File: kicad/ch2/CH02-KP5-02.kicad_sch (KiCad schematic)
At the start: 5 parts

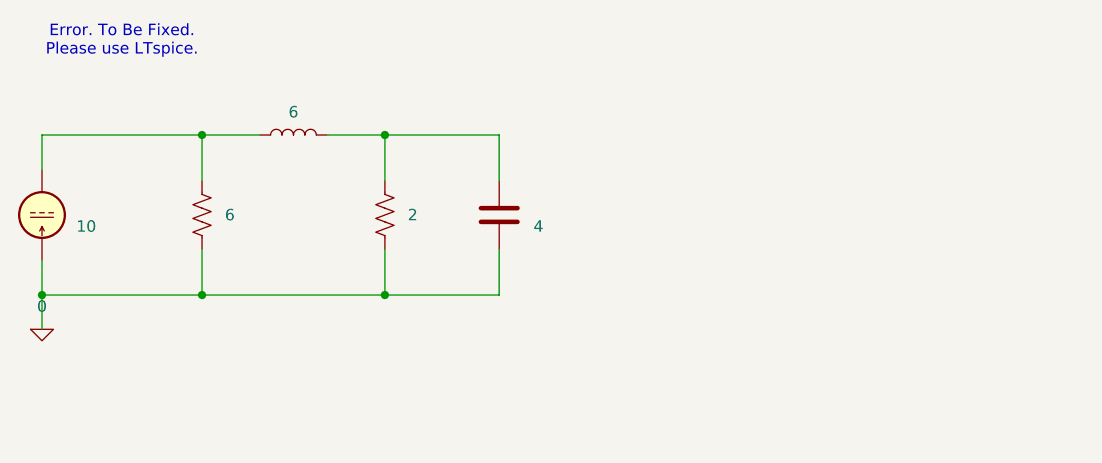
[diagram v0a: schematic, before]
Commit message: fix subsheet sim problem
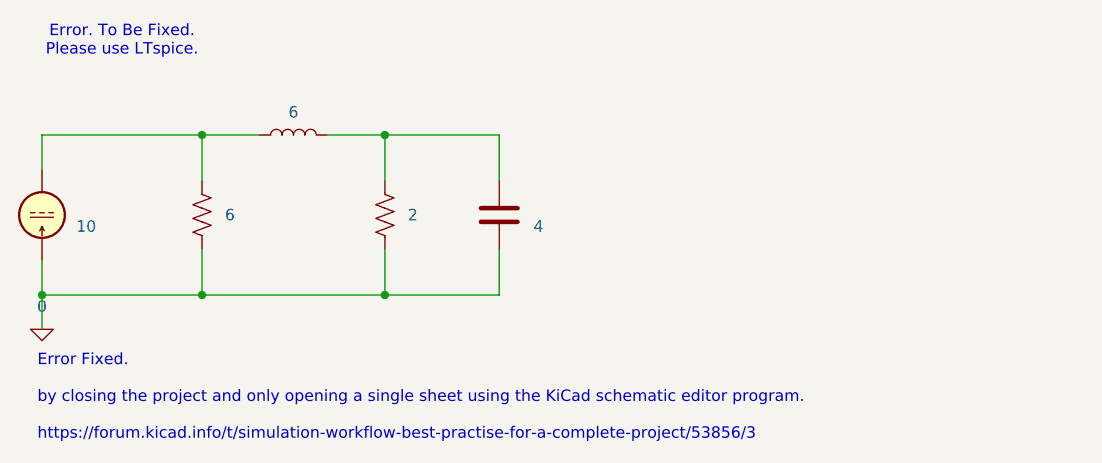
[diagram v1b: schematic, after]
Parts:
- renumbered C5 to C1, I8 to I1, R52 to R1, R53 to R2
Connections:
- net 0: now also R1.2, R2.2; no longer R1.1, R2.1
- net at I1.2, L1.1: now also R1.1; no longer R1.2
- net at C1.1, L1.2: now also R2.1; no longer R2.2
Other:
- note added: "Error Fixed. by closing the project and only opening a single sheet using the KiCad schematic editor program. https://forum.kicad.info/t/simulation-workflow-best-practise-for-a-complete-project/53856/3"
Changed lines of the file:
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@@
+		)
+	)
+	(text "Error Fixed.\n\nby closing the project and only opening a single sheet using the KiCad schematic editor program.\n\nhttps://forum.kicad.info/t/simulation-workflow-best-practise-for-a-complete-project/53856/3"
+		(exclude_from_sim no)
+		(at 50.292 90.17 0)
+		(effects
+			(font
+				(size 1.27 1.27)
+			)
+			(justify left)
 		)
 	)
@@
 	)
 	(symbol
+		(lib_name "R_US_1")
 		(lib_id "Device:R_US")
-		(at 68.58 69.85 180)
+		(at 68.58 69.85 0)
 		(unit 1)
 		(exclude_from_sim no)
@@
 		(dnp no)
 		(fields_autoplaced yes)
-		(property "Reference" "R52"
-			(at 66.04 71.1201 0)
+		(property "Reference" "R1"
+			(at 71.12 68.5799 0)
 			(effects
 				(font
@@
 					(size 1.27 1.27)
 				)
-				(justify right)
+				(justify left)
 			)
 		)
 		(property "Footprint" ""
-			(at 67.564 69.596 90)
+			(at 69.596 70.104 90)
 			(effects
 				(font
@@
 		)
 		(instances
+			(project "CH02-KP5-02"
+				(path "/91953c6e-082e-423a-a84b-0adf7ea4eb58"
+					(reference "R1")
+					(unit 1)
+				)
+			)
 			(project ""
 				(path "/fc72c8c5-f743-437f-8eef-093b2f91e0e9/7f1fd720-65c0-4371-8ff5-0fadc402fcda"
@@
 		(dnp no)
 		(fields_autoplaced yes)
-		(property "Reference" "C5"
+		(property "Reference" "C1"
 			(at 105.41 68.5799 0)
 			(effects
@@
 		)
 		(instances
+			(project "CH02-KP5-02"
+				(path "/91953c6e-082e-423a-a84b-0adf7ea4eb58"
+					(reference "C1")
+					(unit 1)
+				)
+			)
 			(project ""
 				(path "/fc72c8c5-f743-437f-8eef-093b2f91e0e9/7f1fd720-65c0-4371-8ff5-0fadc402fcda"
@@
 		(dnp no)
 		(fields_autoplaced yes)
-		(property "Reference" "I8"
+		(property "Reference" "I1"
 			(at 54.61 68.5799 0)
 			(effects
@@
 		)
 		(instances
+			(project "CH02-KP5-02"
+				(path "/91953c6e-082e-423a-a84b-0adf7ea4eb58"
+					(reference "I1")
+					(unit 1)
+				)
+			)
 			(project ""
 				(path "/fc72c8c5-f743-437f-8eef-093b2f91e0e9/7f1fd720-65c0-4371-8ff5-0fadc402fcda"
@@
 		)
 		(instances
+			(project "CH02-KP5-02"
+				(path "/91953c6e-082e-423a-a84b-0adf7ea4eb58"
+					(reference "L1")
+					(unit 1)
+				)
+			)
 			(project ""
 				(path "/fc72c8c5-f743-437f-8eef-093b2f91e0e9/7f1fd720-65c0-4371-8ff5-0fadc402fcda"
@@
 	(symbol
 		(lib_id "Device:R_US")
-		(at 88.9 69.85 180)
+		(at 88.9 69.85 0)
 		(unit 1)
 		(exclude_from_sim no)
@@
 		(dnp no)
 		(fields_autoplaced yes)
-		(property "Reference" "R53"
-			(at 86.36 71.1201 0)
+		(property "Reference" "R2"
+			(at 91.44 68.5799 0)
 			(effects
 				(font
@@
 					(size 1.27 1.27)
 				)
-				(justify right)
+				(justify left)
 			)
 		)
 		(property "Footprint" ""
-			(at 87.884 69.596 90)
+			(at 89.916 70.104 90)
 			(effects
 				(font
@@
 		)
 		(instances
+			(project "CH02-KP5-02"
+				(path "/91953c6e-082e-423a-a84b-0adf7ea4eb58"
+					(reference "R2")
+					(unit 1)
+				)
+			)
 			(project ""
 				(path "/fc72c8c5-f743-437f-8eef-093b2f91e0e9/7f1fd720-65c0-4371-8ff5-0fadc402fcda"
@@
 		(dnp no)
 		(fields_autoplaced yes)
-		(property "Reference" "#GND016"
+		(property "Reference" "#GND0101"
 			(at 50.8 87.63 0)
 			(effects
@@
 		)
 		(instances
+			(project "CH02-KP5-02"
+				(path "/91953c6e-082e-423a-a84b-0adf7ea4eb58"
+					(reference "#GND0101")
+					(unit 1)
+				)
+			)
 			(project ""
 				(path "/fc72c8c5-f743-437f-8eef-093b2f91e0e9/7f1fd720-65c0-4371-8ff5-0fadc402fcda"
@@
 		)
 	)
+	(sheet_instances
+		(path "/"
+			(page "1")
+		)
+	)
+	(embedded_fonts no)
 )
